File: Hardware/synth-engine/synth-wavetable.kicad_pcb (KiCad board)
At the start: 2 copper layers, 196 parts, among them J1 SWD_programming, J2 USB, J3 MIDI_IN, J4 MIDI_OUT, J5 SWD_JTAG, J6 AUDIO-JACK4-.25-HORIZ-TRS, J7 Conn_01x02, U1 CY8C4246AZI-L445, U10 NJM4580, U11 NJM4580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

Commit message: rough placement and symbol organization. If I need to start PCB layout over from scracth, revert to this commit.
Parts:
- removed U11: NJM4580, SparkFun-DigitalIC:SO08
- added Q1: 2N3904, SparkFun-DiscreteSemi:SOT23-3, F.Cu at (36.0, 178.0)
- added U4: TL074CN, SparkFun-AnalogIC:SOIC8, F.Cu at (251.0, 108.0)
- added U5: SSI2144, SparkFun-AnalogIC:SSOP16, F.Cu at (232.0, 107.0)
- added U6: V7805-1000, SparkFun-DiscreteSemi:DPAK, F.Cu at (41.0, 10.0)
- J7: footprint SparkFun-Connectors:1X02 -> SparkFun-Connectors:POWER_JACK_SLOT
- moved J6 254.5 mm to (348.0, 107.0), turned to 180 degrees
- moved RV17 221.5 mm to (306.0, 107.0), turned to 90 degrees
- moved RV3 211.2 mm to (-75.0, 143.0), turned to 90 degrees
- moved R13 201.1 mm to (-80.0, 148.0), turned to 270 degrees
- moved RV6 199.9 mm to (-58.0, 143.0), turned to 90 degrees
- moved R12 193.8 mm to (-75.0, 148.0), turned to 90 degrees
- moved RV1 185.6 mm to (-68.0, 53.0), turned to 90 degrees
- moved J7 185.1 mm to (22.0, 6.00), turned to 180 degrees
- moved C17 184.2 mm to (-60.0, 148.0), turned to 270 degrees
- moved R11 183.4 mm to (-69.0, 106.0)
- moved R9 183.2 mm to (-73.0, 58.1), turned to 270 degrees
- moved R56 183.2 mm to (267.0, 112.0), turned to 180 degrees
- moved R19 181.5 mm to (-63.0, 148.0), turned to 270 degrees
- moved R49 176.7 mm to (261.0, 71.0), turned to 270 degrees
- moved R8 175.8 mm to (-68.0, 58.0), turned to 90 degrees
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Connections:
- U10 pad 5: (no net) -> Net-(C80-Pad2)
- U10 pad 6: (no net) -> Net-(C82-Pad2)
- U10 pad 7: (no net) -> Net-(C82-Pad1)

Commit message: route 3.3VD voltage regulator and control MCU
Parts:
- moved U8 109.3 mm to (129.9, -12.3), turned to 180 degrees
- moved C60 108.9 mm to (130.1, -9.00), turned to 180 degrees
- moved C52 106.1 mm to (129.9, -20.0)
- moved C55 105.5 mm to (129.9, -16.0)
- moved C57 105.4 mm to (124.0, -18.0), turned to 90 degrees
- moved FB2 104.1 mm to (129.9, -18.0)
- moved R59 88.7 mm to (5.25, 23.6), turned to 90 degrees
- moved J1 71.5 mm to (55.6, 11.5), turned to 0 degrees
- moved J2 71.3 mm to (40.0, 14.0)
- moved C11 63.8 mm to (11.0, 45.8)
- moved C10 61.3 mm to (13.0, 52.9)
- moved C4 60.9 mm to (16.4, 54.8)
- moved R1 60.7 mm to (11.0, 43.1)
- moved C1 60.7 mm to (30.0, 44.0)
- moved C3 60.7 mm to (20.0, 53.0)
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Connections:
- C1 pad 1: +5V -> 3.3V
- C3 pad 1: +5V -> 3.3V
- C4 pad 1: +5V -> 3.3V
- C5 pad 1: +5V -> 3.3V
- C6 pad 2: +5V -> 3.3V
- C7 pad 1: +5V -> 3.3V
- C8 pad 1: +5V -> 3.3V
- C9 pad 2: +5V -> 3.3V
- J1 pad 1: +5V -> 3.3V
- R2 pad 1: +5V -> 3.3V
- U1 pad 11: +5V -> 3.3V
- U1 pad 17: +5V -> 3.3V
- U1 pad 50: +5V -> 3.3V
- U1 pad 56: +5V -> 3.3V
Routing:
- net GNDD: track 0.00 -> 145.8 mm, vias 0 -> 3
- net 3.3V: track 0.00 -> 122.4 mm, vias 0 -> 5
- net /Control/XRES: track 0.00 -> 74.4 mm, vias 0 -> 1
- net /Control/SDAT: track 0.00 -> 55.6 mm, vias 0 -> 1
- net /Control/SCLK: track 0.00 -> 54.9 mm, vias 0 -> 1
- net GND: track 0.00 -> 17.8 mm
- net Net-(C54-Pad1): track 0.00 -> 14.3 mm
- net Net-(C2-Pad1): track 0.00 -> 13.4 mm
- net Net-(C11-Pad1): track 0.00 -> 13.3 mm
- net +5V: track 0.00 -> 11.4 mm
- net (no net): track 0.00 -> 5.30 mm
- net Net-(C10-Pad1): track 0.00 -> 4.18 mm
- net +15V: track 0.00 -> 2.95 mm

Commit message: route STM32 bypass caps and programming header
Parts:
- moved J6 224.0 mm to (154.0, -5.00), turned to 270 degrees
- moved RV17 201.2 mm to (127.8, 13.5)
- moved C50 157.4 mm to (234.0, -16.2)
- moved R57 157.4 mm to (232.7, -24.3)
- moved R58 157.4 mm to (234.2, -23.0)
- moved C49 146.5 mm to (138.0, 35.5), turned to 90 degrees
- moved R56 144.0 mm to (145.0, 35.5), turned to 270 degrees
- moved R55 127.6 mm to (133.0, 51.5), turned to 90 degrees
- moved C48 126.6 mm to (135.0, 51.4), turned to 90 degrees
- moved U4 123.7 mm to (141.0, 51.5), turned to 90 degrees
- moved R52 110.3 mm to (136.0, 63.5), turned to 90 degrees
- moved R53 109.2 mm to (138.0, 63.5), turned to 90 degrees
- moved C43 106.4 mm to (140.9, 64.5), turned to 0 degrees
- moved R46 106.0 mm to (131.0, 69.4), turned to 90 degrees
- moved C44 104.9 mm to (144.0, 64.5), turned to 0 degrees
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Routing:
- net 3.3V: track 122.4 -> 339.7 mm, vias 5 -> 9
- net GNDD: track 145.8 -> 334.7 mm, vias 3 -> 12
- net /Audio Engine/NRST: track 0.00 -> 118.0 mm, vias 0 -> 3
- net /Audio Engine/SWO: track 0.00 -> 114.9 mm, vias 0 -> 2
- net /Audio Engine/SWCLK: track 0.00 -> 106.3 mm, vias 0 -> 2
- net /Audio Engine/SWDIO: track 0.00 -> 97.4 mm, vias 0 -> 2
- net Net-(C24-Pad1): track 0.00 -> 19.3 mm, vias 0 -> 2
- net Net-(C25-Pad1): track 0.00 -> 19.0 mm, vias 0 -> 2
- net /Control/XRES: track 74.4 -> 83.7 mm
- net /Control/SCLK: track 54.9 -> 64.2 mm
- net /Control/SDAT: track 55.6 -> 64.8 mm
- net Net-(C26-Pad1): track 0.00 -> 8.25 mm
- net +3.3VA: track 0.00 -> 7.75 mm
- net GND: track 17.8 -> 25.1 mm
- net Net-(R32-Pad1): track 0.00 -> 6.66 mm
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
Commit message: add separate PCB with potentiometers and switches and connector between control board and synth engine
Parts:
- removed C12, C13, C14, C15, C16, C17, C18, C19, C20, C21, C22, C23: C_Small, SparkFun-Passives:0805
- removed R10, R11, R12, R13, R14, R15, R16, R17, R18, R19, R20, R21, R22, R23, R24, R25, R26, R27, R28, R29, R30, R31, R8, R9: 0, SparkFun-Passives:0805
- removed RV1, RV10, RV11, RV12, RV2, RV3, RV4, RV5, RV6, RV7, RV8, RV9: 20kB, Potentiometer_THT:Potentiometer_Alps_RK09K_Single_Vertical
- added J8: Conn_02x12_Odd_Even, SparkFun-Connectors:2X12, F.Cu at (3.73, 74.3)
- D2: value D_Schottky -> 1N5711; footprint SparkFun-DiscreteSemi:SMA-DIODE -> SparkFun-Passives:1210
- J2: value USB -> USB-B-S
- J7: value Conn_01x02 -> POWER_JACKPTH; footprint SparkFun-Connectors:POWER_JACK_SLOT -> SparkFun-Connectors:POWER_JACK_PTH
- U4: footprint SparkFun-AnalogIC:SOIC8 -> SparkFun-AnalogIC:SO16
- moved R58 190.8 mm to (52.5, 35.2), turned to 270 degrees
- moved R57 188.8 mm to (52.5, 32.0), turned to 270 degrees
- moved C50 184.5 mm to (57.2, 36.5), turned to 270 degrees
- moved R44 170.7 mm to (65.0, 44.8)
- moved R43 129.9 mm to (119.0, 104.2)
- moved R45 129.9 mm to (119.0, 100.4)
- moved R49 129.9 mm to (134.0, 98.2)
- moved RV15 129.9 mm to (119.0, 93.2)
- moved RV16 129.9 mm to (136.0, 93.2)
- moved C52 103.5 mm to (52.9, 44.5), turned to 0 degrees
- moved C55 103.5 mm to (52.9, 48.5)
- moved C57 103.5 mm to (47.0, 46.5)
- moved C60 103.5 mm to (53.1, 55.5)
- moved FB2 103.5 mm to (52.9, 46.5), turned to 180 degrees
- moved U8 103.5 mm to (52.9, 52.2)
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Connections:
- net Net-(U1-Pad27) renamed /Connectors/release
- net Net-(U1-Pad28) renamed /Connectors/lfo_rate
- net Net-(U1-Pad29) renamed /Connectors/lfo_depth
- net Net-(U1-Pad30) renamed /Connectors/global_lfo_rate
- net Net-(U1-Pad31) renamed /Connectors/global_lfo_depth
- J2 pad D+: (no net) -> Net-(J2-PadD+)
- J2 pad D-: (no net) -> Net-(J2-PadD-)
- J2 pad GND: (no net) -> GNDD
- J7 pad PWR: (no net) -> Net-(D2-Pad2)
- U1 pad 18: Net-(U1-Pad18) -> /Connectors/osc1_waveshape
- U1 pad 19: Net-(U1-Pad19) -> /Connectors/osc2_tune
- U1 pad 22: Net-(U1-Pad22) -> /Connectors/osc2_waveshape
- U1 pad 23: Net-(U1-Pad23) -> /Connectors/attack
- U1 pad 24: Net-(U1-Pad24) -> /Connectors/decay
- U1 pad 25: Net-(U1-Pad25) -> /Connectors/sustain
- U1 pad 32: Net-(U1-Pad32) -> /Control/MIDI_IN
- U1 pad 33: Net-(U1-Pad33) -> /Control/MIDI_OUT
- U1 pad 34: Net-(J2-Pad3) -> Net-(J2-PadD+)
- U1 pad 35: Net-(J2-Pad2) -> Net-(J2-PadD-)
- U1 pad 7: Net-(U1-Pad7) -> /Audio Engine/UART_RX
- U1 pad 8: Net-(U1-Pad8) -> /Control/UART_RX
- U1 pad 9: Net-(U1-Pad9) -> /Connectors/osc1_tune
- U3 pad 38: /Audio Engine/PDN -> /Audio Engine/I2S_WCLK
- U3 pad 39: /Audio Engine/CSN -> /Audio Engine/CAD1
- U3 pad 40: /Audio Engine/DIF0 -> /Audio Engine/DIF2
- U3 pad 42: /Audio Engine/DIF2 -> /Audio Engine/DIF0
- U3 pad 43: /Audio Engine/CAD1 -> /Audio Engine/CSN
- U3 pad 44: /Audio Engine/I2S_WCLK -> /Audio Engine/PDN
- U4 pad 4: GND -> +15V
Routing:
- net +15V: track 2.95 -> 238.3 mm, vias 0 -> 3
- net VREF: track 0.00 -> 212.1 mm, vias 0 -> 6
- net +5V: track 11.4 -> 205.3 mm, vias 0 -> 7
- net 3.3V: track 339.7 -> 454.4 mm, vias 9 -> 14
- net GND: track 25.1 -> 105.6 mm, vias 0 -> 1
- net +3.3VA: track 7.75 -> 78.9 mm, vias 0 -> 2
- net /Audio Engine/I2C_SCL: track 0.00 -> 66.9 mm, vias 0 -> 1
- net /Audio Engine/I2C_SDA: track 0.00 -> 64.0 mm, vias 0 -> 2
- net GNDD: track 334.7 -> 389.0 mm, vias 12 -> 14
- net Net-(J2-PadD-): track 0.00 -> 52.1 mm, vias 0 -> 3
- net Net-(J2-PadD+): track 0.00 -> 46.1 mm, vias 0 -> 3
- net /Audio Engine/MCLK: track 0.00 -> 38.4 mm, vias 0 -> 2
- net Net-(C48-Pad2): track 0.00 -> 37.1 mm, vias 0 -> 2
- net (no net): track 5.30 -> 39.2 mm, vias 0 -> 3
- net Net-(C48-Pad1): track 0.00 -> 33.5 mm, vias 0 -> 2
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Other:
- board outline added: 100 x 100 mm

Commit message: route control board
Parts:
- moved J8 0.24 mm to (3.73, 74.0)
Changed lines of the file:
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@@
   )
   (module SparkFun-Connectors:2X12 (layer F.Cu)
-    (at 3.73 74.27 90)
+    (at 3.73 74.03 90)
     (attr virtual)
     (fp_text reference J8 (at -12.065 -3.81 90) (layer B.SilkS)

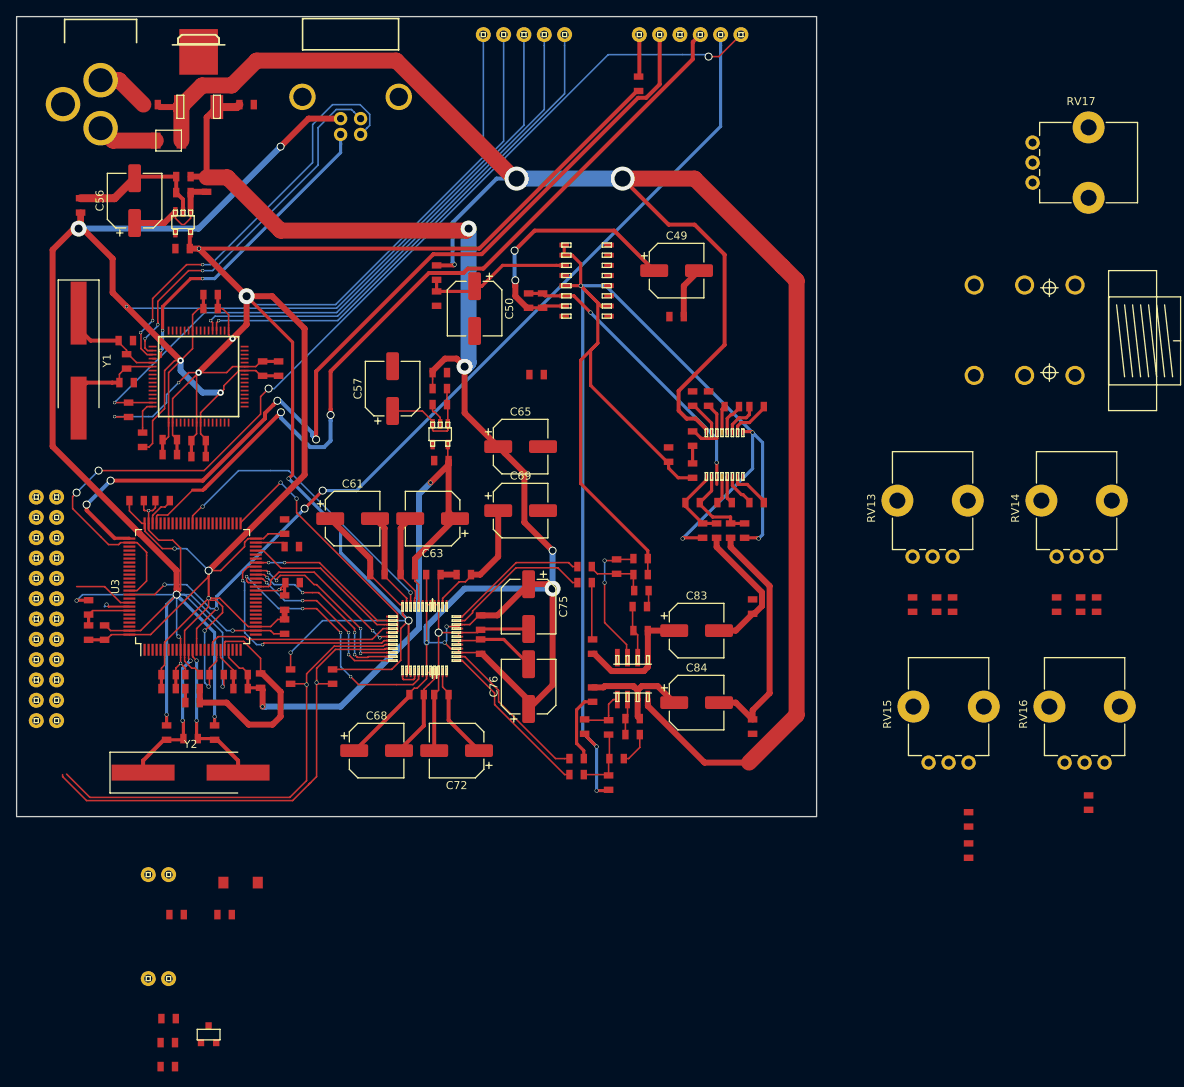
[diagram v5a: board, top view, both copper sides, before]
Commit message: initial routing complete. Still need to do ground plane pours. There are still some issues with incorrect footprints.
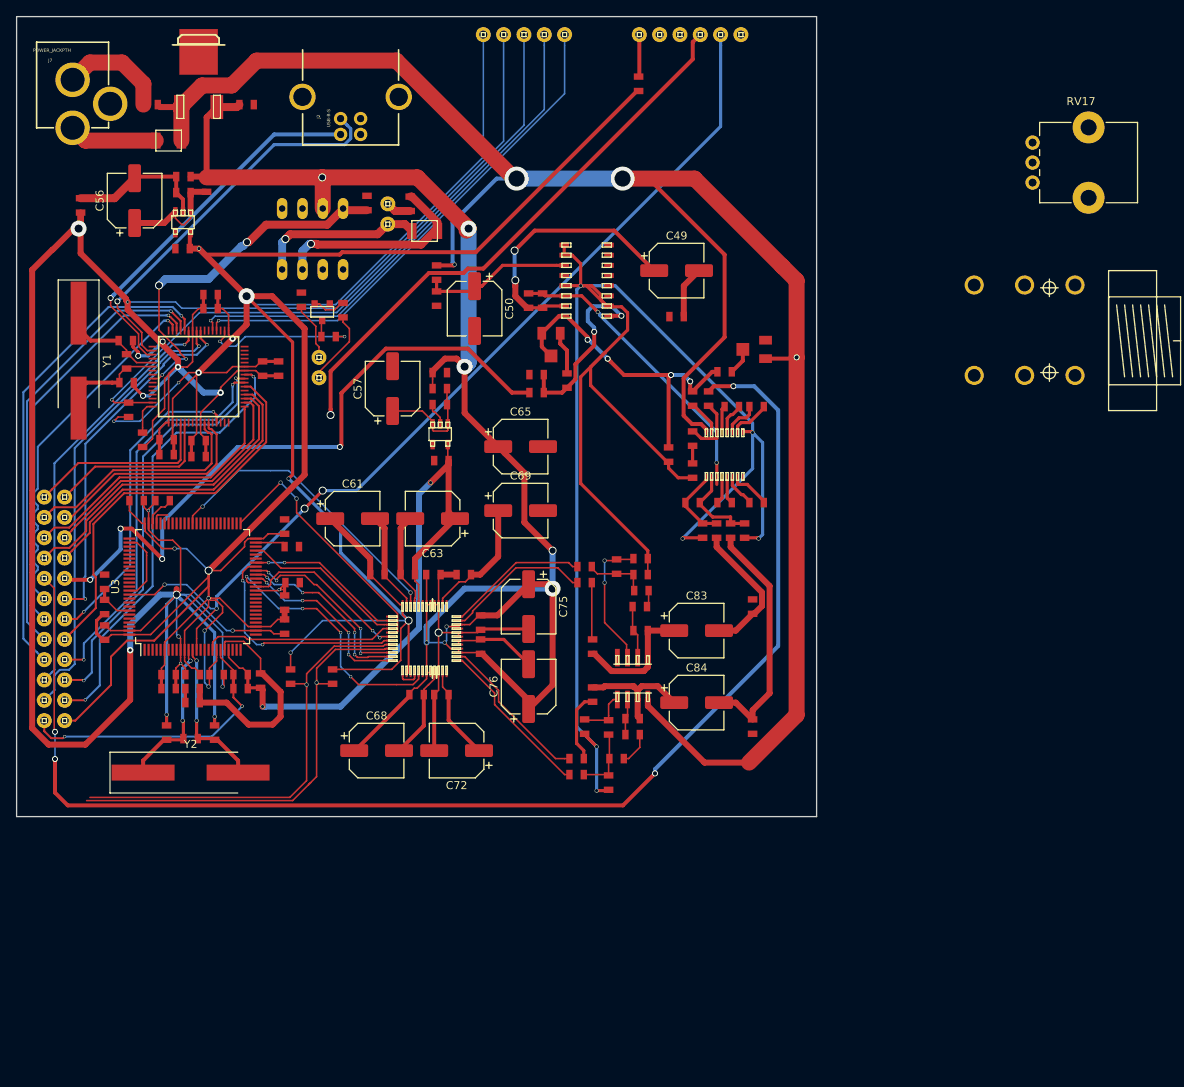
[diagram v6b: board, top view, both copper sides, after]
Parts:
- removed C40, C41: C_Small, SparkFun-Passives:0805
- removed R39, R40, R41, R42: R, SparkFun-Passives:0805
- removed RV13, RV14: 20k, Potentiometer_THT:Potentiometer_Alps_RK09K_Single_Vertical
- added U2: 4N28, SparkFun-AnalogIC:DIL-08, F.Cu at (37.0, 27.8)
- D1: footprint SparkFun-DiscreteSemi:SMA-DIODE -> SparkFun-Passives:1210
- J2, J7: moved to B.Cu
- RV15, RV16: footprint Potentiometer_THT:Potentiometer_Alps_RK09K_Single_Vertical -> SparkFun-Electromechanical:TRIMPOT-3MM-2
- moved R7 97.1 mm to (40.8, 36.7), turned to 90 degrees
- moved R6 94.3 mm to (35.6, 35.4), turned to 90 degrees
- moved R3 93.5 mm to (49.2, 23.4), turned to 270 degrees
- moved Q1 91.5 mm to (38.2, 36.9), turned to 180 degrees
- moved R4 90.7 mm to (43.8, 23.3), turned to 90 degrees
- moved R5 87.6 mm to (39.0, 40.0)
- moved J3 86.6 mm to (46.4, 25.9), turned to 90 degrees
- moved D1 84.6 mm to (51.0, 26.8)
- moved J4 80.5 mm to (37.8, 42.6), turned to 270 degrees
- moved R43 78.7 mm to (65.0, 47.0), turned to 180 degrees
- moved R45 74.4 mm to (68.8, 45.5)
- moved RV15 73.9 mm to (66.8, 41.0), turned to 180 degrees
- moved R49 70.5 mm to (88.5, 44.4), turned to 180 degrees
- moved RV16 67.7 mm to (92.2, 41.6)
- moved R32 3.77 mm to (11.0, 73.8)
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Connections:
- net Net-(U1-Pad13) renamed /Control/UART_TX
- net Net-(U1-Pad39) renamed /Control/FREQ_CTRL
- J8 pad 1: +3V3 -> 3.3V
- J8 pad 10: Net-(J8-Pad10) -> /Connectors/lfo_depth
- J8 pad 12: Net-(J8-Pad12) -> /Connectors/global_lfo_rate
- J8 pad 14: Net-(J8-Pad14) -> /Connectors/global_lfo_depth
- J8 pad 15: +3V3 -> /Connectors/filter_freq
- J8 pad 16: GND -> /Connectors/filter_resonance
- J8 pad 17: Net-(J8-Pad17) -> /Connectors/mod1
- J8 pad 18: Net-(J8-Pad18) -> /Connectors/mod2
- J8 pad 19: Net-(J8-Pad19) -> /Connectors/mod3
- J8 pad 2: Net-(J8-Pad2) -> GND
- J8 pad 20: Net-(J8-Pad20) -> /Connectors/mod4
- J8 pad 21: Net-(J8-Pad21) -> /Connectors/mod5
- J8 pad 22: Net-(J8-Pad22) -> /Connectors/mod6
- J8 pad 23: Net-(J8-Pad23) -> /Connectors/mod7
- J8 pad 24: Net-(J8-Pad24) -> /Connectors/mod8
- J8 pad 6: Net-(J8-Pad6) -> /Connectors/release
- J8 pad 8: Net-(J8-Pad8) -> /Connectors/lfo_rate
- R43 pad 2: Net-(C40-Pad1) -> /Connectors/filter_freq
- R53 pad 2: /Filter/Q_CTRL -> /Connectors/filter_resonance
- U1 pad 1: Net-(U1-Pad1) -> /Connectors/mod4
- U1 pad 12: Net-(U1-Pad12) -> /Control/UART_RX
- U1 pad 18: /Connectors/osc1_waveshape -> /Control/MIDI_OUT
- U1 pad 19: /Connectors/osc2_tune -> Net-(U1-Pad19)
- U1 pad 2: Net-(U1-Pad2) -> /Connectors/mod3
- U1 pad 22: /Connectors/osc2_waveshape -> Net-(U1-Pad22)
- U1 pad 23: /Connectors/attack -> Net-(U1-Pad23)
- U1 pad 3: Net-(U1-Pad3) -> /Connectors/mod2
- U1 pad 32: /Control/MIDI_IN -> Net-(U1-Pad32)
- U1 pad 33: /Control/MIDI_OUT -> Net-(U1-Pad33)
- U1 pad 4: Net-(U1-Pad4) -> /Connectors/mod1
- U1 pad 41: Net-(U1-Pad41) -> /Control/MIDI_IN
- U1 pad 52: Net-(U1-Pad52) -> /Connectors/mod8
- U1 pad 53: Net-(U1-Pad53) -> /Connectors/mod7
- U1 pad 58: Net-(U1-Pad58) -> /Connectors/mod6
- U1 pad 59: Net-(U1-Pad59) -> /Connectors/mod5
- U1 pad 6: Net-(U1-Pad6) -> /Connectors/osc2_waveshape
- U1 pad 61: Net-(U1-Pad61) -> /Connectors/attack
- U1 pad 7: /Audio Engine/UART_RX -> /Connectors/osc2_tune
- U1 pad 8: /Control/UART_RX -> /Connectors/osc1_waveshape
- U3 pad 23: /Control/UART_RX -> /Audio Engine/UART_TX
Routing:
- net /Connectors/filter_resonance: track 0.00 -> 166.6 mm, vias 0 -> 4
- net /Audio Engine/SWO: track 128.4 -> 8.89 mm, vias 4 -> 0
- net /Audio Engine/SWCLK: track 116.7 -> 0.00 mm, vias 4 -> 0
- net /Connectors/filter_freq: track 0.00 -> 83.6 mm, vias 0 -> 4
- net /Connectors/lfo_rate: track 0.00 -> 61.2 mm, vias 0 -> 1
- net /Connectors/sustain: track 0.00 -> 56.7 mm, vias 0 -> 1
- net /Connectors/lfo_depth: track 0.00 -> 56.3 mm, vias 0 -> 1
- net /Connectors/osc1_tune: track 0.00 -> 56.3 mm, vias 0 -> 2
- net /Connectors/global_lfo_rate: track 0.00 -> 52.9 mm, vias 0 -> 1
- net /Connectors/osc1_waveshape: track 0.00 -> 52.4 mm, vias 0 -> 2
- net /Connectors/release: track 0.00 -> 52.0 mm, vias 0 -> 1
- net /Connectors/osc2_waveshape: track 0.00 -> 50.5 mm
- net /Connectors/osc2_tune: track 0.00 -> 49.5 mm, vias 0 -> 2
- net /Control/MIDI_IN: track 0.00 -> 45.9 mm, vias 0 -> 4
- net /Connectors/global_lfo_depth: track 0.00 -> 45.5 mm, vias 0 -> 1
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
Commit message: add ground plane copper pours
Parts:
- removed J6: AUDIO-JACK4-.25-HORIZ-TRS, SparkFun-Connectors:AUDIO-JACK-.25-INCH-HORIZ-PTH
- removed RV17: 50k, Potentiometer_THT:Potentiometer_Alps_RK09K_Single_Vertical
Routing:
- net GNDD: track 394.6 -> 577.5 mm, vias 16 -> 26
- net /Audio Engine/SWO: track 8.89 -> 121.1 mm, vias 0 -> 4
- net /Audio Engine/SWCLK: track 0.00 -> 109.1 mm, vias 0 -> 4
- net GND: track 143.2 -> 233.6 mm, vias 3 -> 25
- net +15V: track 241.8 -> 275.5 mm, vias 4 -> 7
- net +5V: track 209.4 -> 239.4 mm, vias 8 -> 9
- net /Audio Engine/SWDIO: track 72.7 -> 100.5 mm, vias 1 -> 2
- net /Audio Engine/I2C_SCL: track 55.4 -> 48.4 mm, vias 1 -> 4
- net /Audio Engine/I2C_SDA: track 56.2 -> 49.3 mm, vias 1 -> 4
- net 3.3V: track 486.2 -> 483.6 mm
- net /Control/MIDI_OUT: track 19.0 -> 18.0 mm
- net Net-(C48-Pad1): track 33.5 -> 32.9 mm
- net /Audio Engine/NRST: track 119.2 -> 119.7 mm
- net Net-(J4-Pad2): track 9.45 -> 8.90 mm
- added copper zone on B.Cu, net GND
- added copper zone on F.Cu, net GND
